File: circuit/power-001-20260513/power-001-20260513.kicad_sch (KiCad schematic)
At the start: 47 parts, among them J1 VIN, Q1 NMOS, Q2 PMOS, SW1 SW_SPST, SW2 SW_SPDT, SW3 SW_SPDT, SW4 SW_SPDT, U1 PIC12F683-xSN

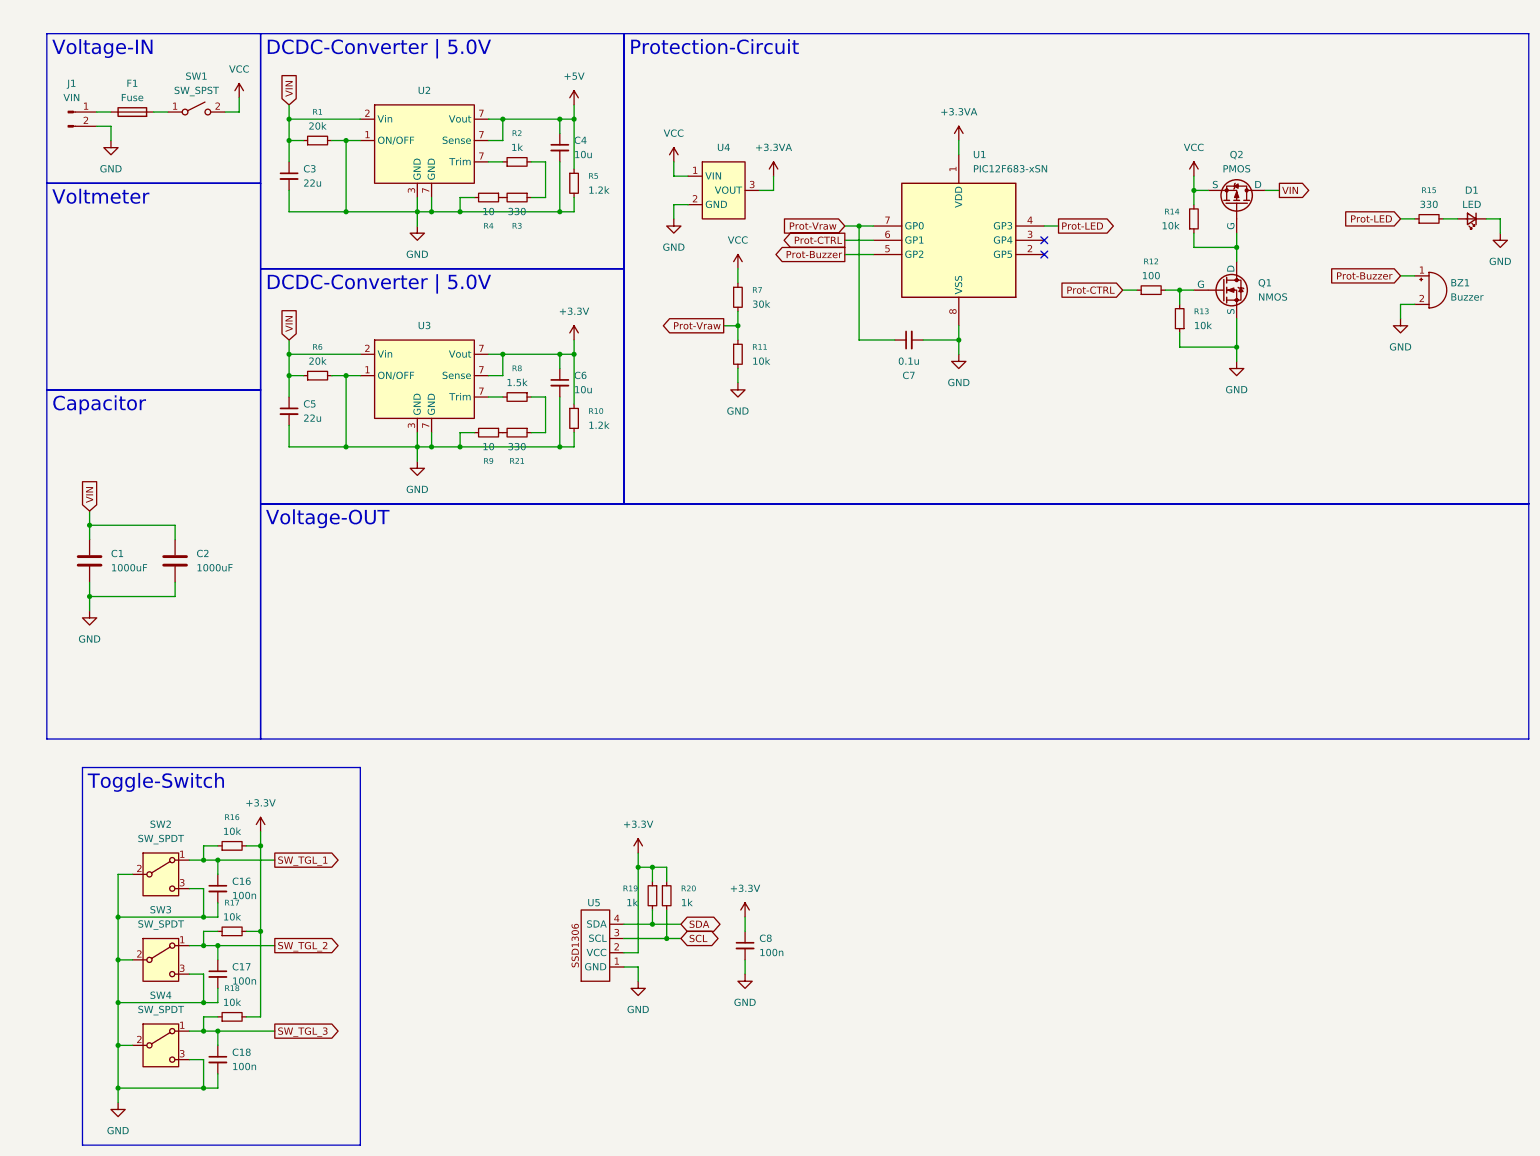
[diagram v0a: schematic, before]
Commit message: Update 電源基板の回路図完成・OKLのシンボルのピン番号が被っていたので修正
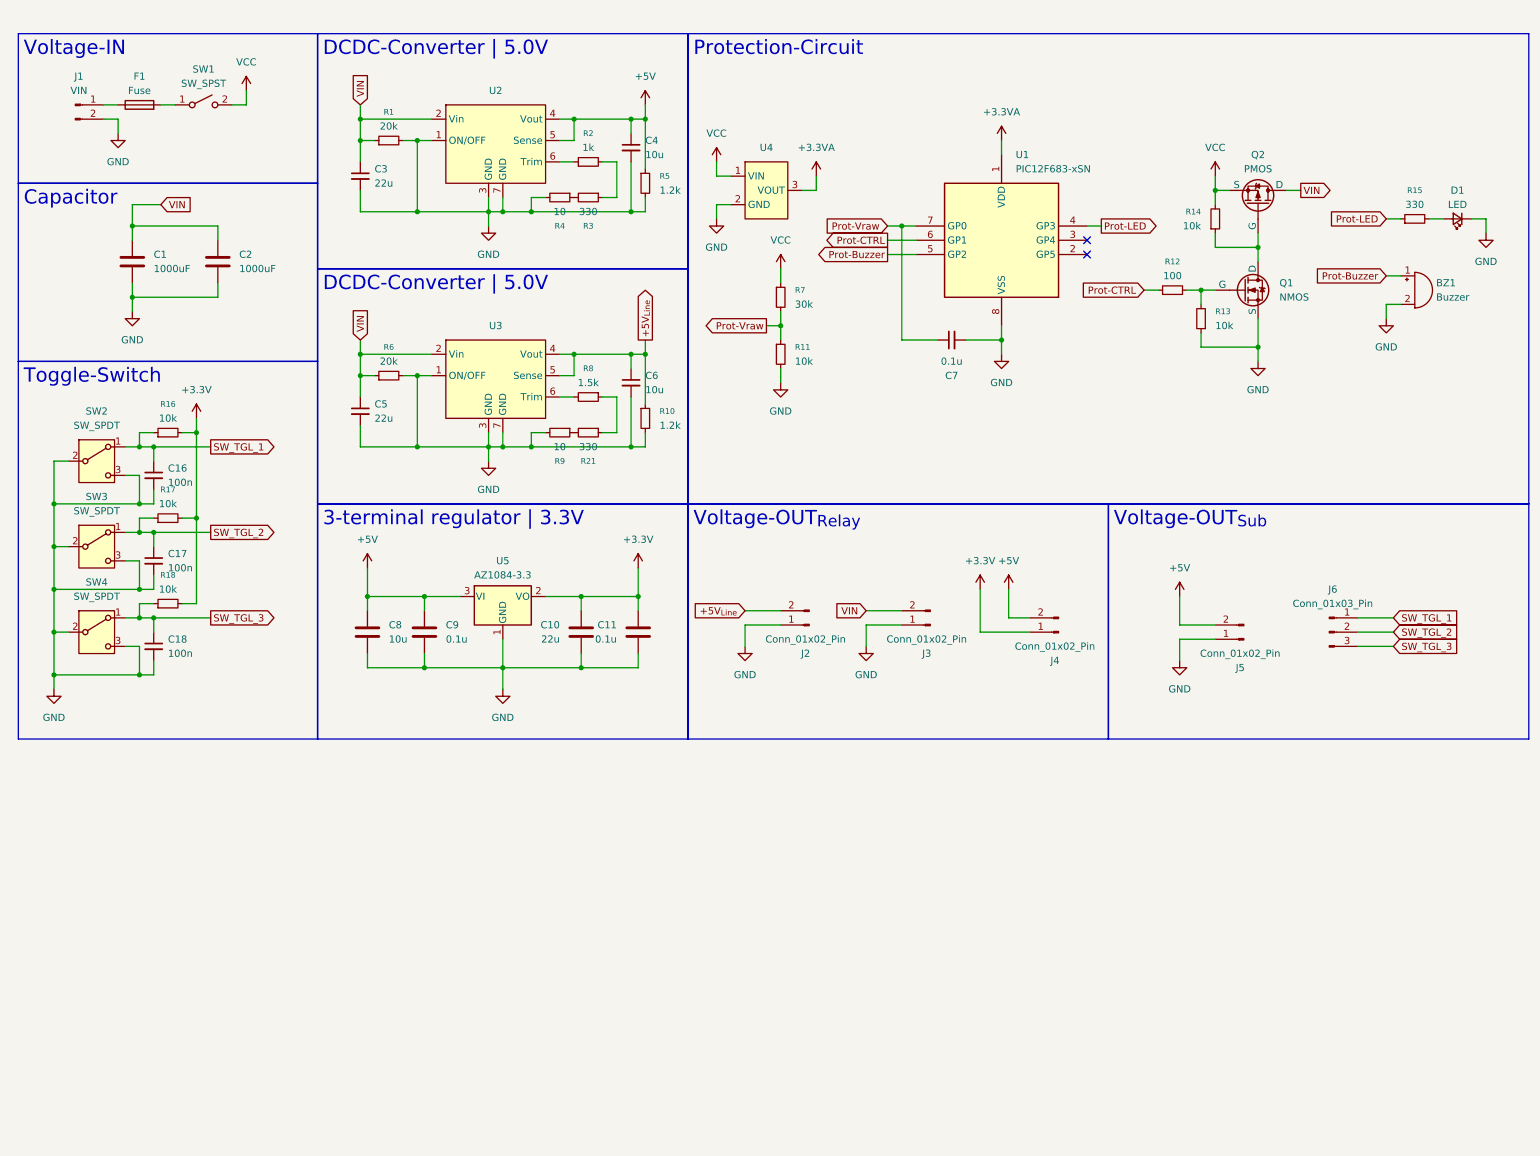
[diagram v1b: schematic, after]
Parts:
- removed C8: 100n, Capacitor_SMD:C_0805_2012Metric, symbol Device:C_Small
- removed R19, R20: 1k, Resistor_SMD:R_0805_2012Metric, symbol Device:R_Small
- removed U5: (no value), symbol @Thrive_symbol_sub:SSD1306
- added C10: 22u, symbol Device:C
- added C11, C9: 0.1u, symbol Device:C
- added C8: 10u, symbol Device:C
- added J2, J3, J4, J5: Conn_01x02_Pin, symbol Connector:Conn_01x02_Pin
- added J6: Conn_01x03_Pin, symbol Connector:Conn_01x03_Pin
- added U5: AZ1084-3.3, symbol Regulator_Linear:AZ1084-3.3
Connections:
- net +3.3V: now also C10.1, C11.1, J4.1 (Pin_1), U5.2 (VO); no longer C6.1, R10.1, U3.7 (Trim)
- net +5V: now also U2.4 (Vout), U2.5 (Sense), C8.1, C9.1, J4.2 (Pin_2), J5.2 (Pin_2), U5.3 (VI); no longer U2.7 (Trim)
- net GND: now also C10.2, C11.2, C8.2, C9.2, J2.1 (Pin_1), J3.1 (Pin_1), J5.1 (Pin_1), U5.1 (GND)
- net SW_TGL_1: now also J6.1 (Pin_1)
- net SW_TGL_2: now also J6.2 (Pin_2)
- net SW_TGL_3: now also J6.3 (Pin_3)
- net VIN: now also J3.2 (Pin_2)
- net at R2.1: now also U2.6 (Trim); no longer U2.7 (Trim)
- net at R8.2: now also U3.6 (Trim); no longer U3.7 (Trim)
- new net +5V_{Line}: C6.1, J2.2 (Pin_2), R10.1, U3.4 (Vout), U3.5 (Sense)
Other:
- moved on the sheet: BZ1, C1, C16, C17, C18, C2, C3, C4, C5, C6, C7, D1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

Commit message: Update 電源基板をちょっと進めた
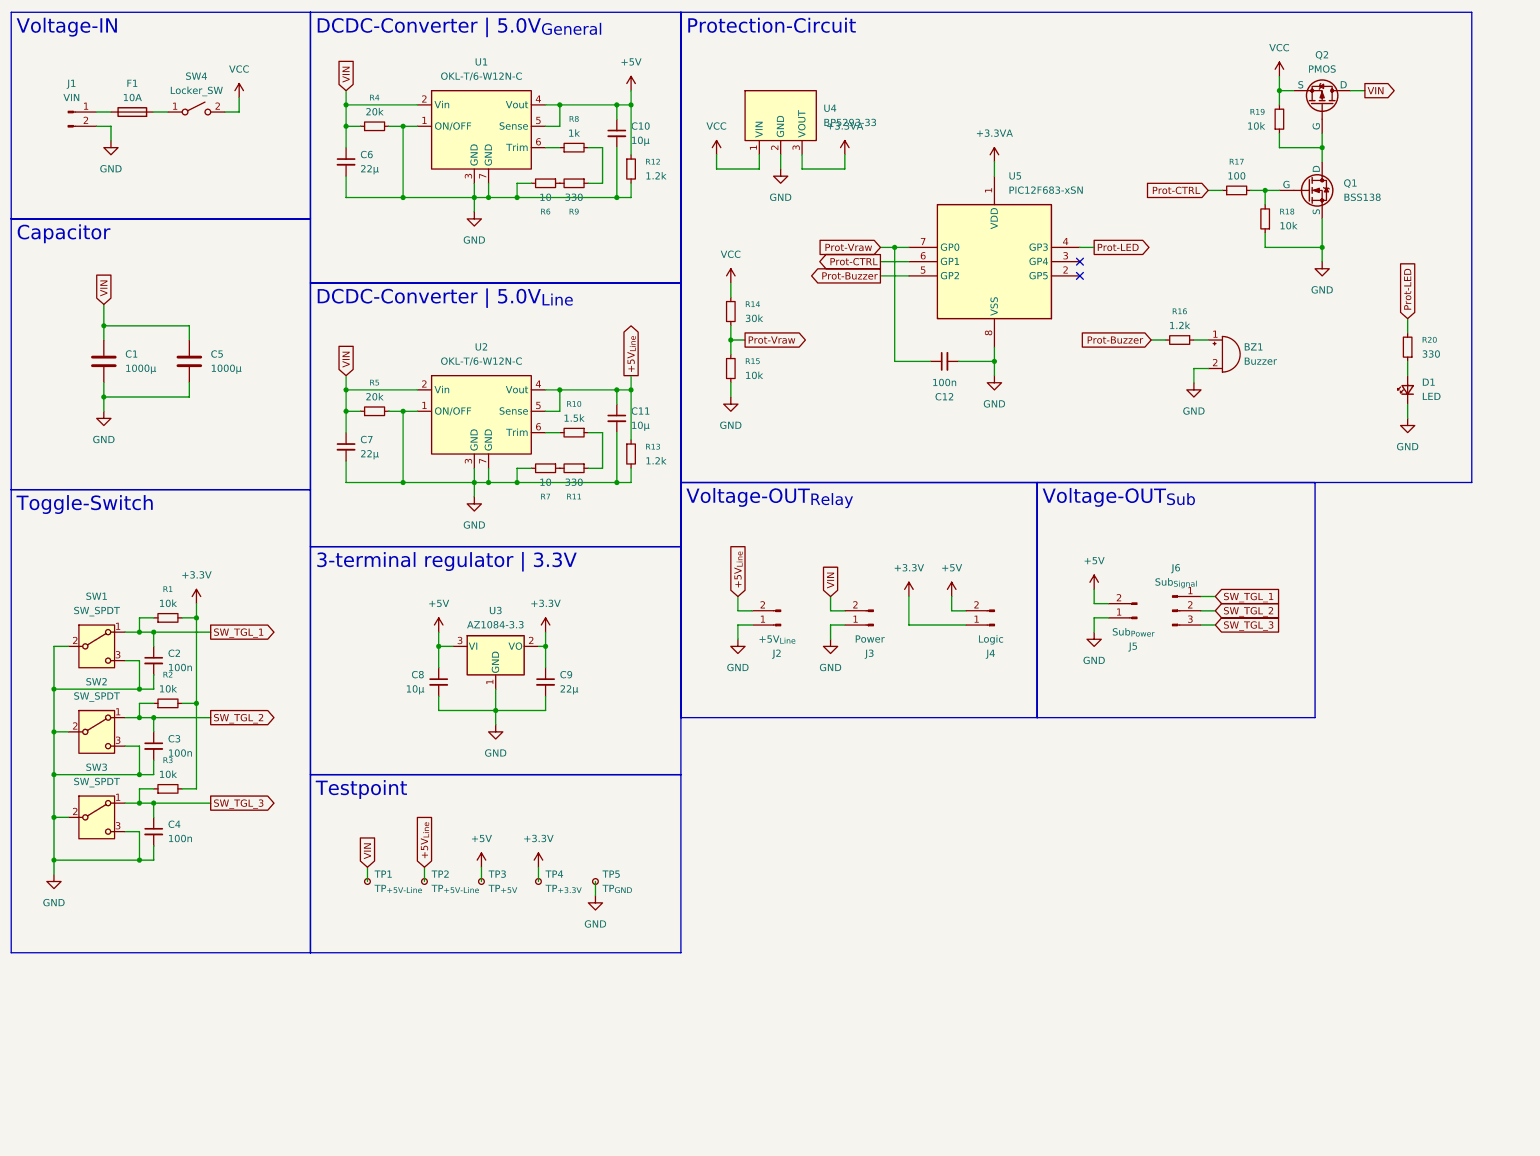
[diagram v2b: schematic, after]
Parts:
- removed C10: 22u, symbol Device:C
- removed C11, C9: 0.1u, symbol Device:C
- removed C8: 10u, symbol Device:C
- removed U3: (no value), symbol @Thrive_symbol_power:OKL-T/6-W12N-C
- added C8: 10μ, Capacitor_SMD:C_0805_2012Metric, symbol Device:C_Small
- added C9: 22μ, Capacitor_SMD:C_0805_2012Metric, symbol Device:C_Small
- added R16: 1.2k, Resistor_SMD:R_0805_2012Metric, symbol Device:R_Small
- added TP1, TP2: TP_{+5V-Line}, symbol Connector:TestPoint_Small
- added TP3: TP_{+5V}, symbol Connector:TestPoint_Small
- added TP4: TP_{+3.3V}, symbol Connector:TestPoint_Small
- added TP5: TP_{GND}, symbol Connector:TestPoint_Small
- added U1: OKL-T/6-W12N-C, @Thrive_footprint_power:OKL-T6-W12N-C, symbol @Thrive_symbol_power:OKL-T/6-W12N-C
- BZ1: footprint (none) -> @Thrive_footprint_power:PKM13EPYH4000-A0
- C1: value 1000uF -> 1000μ
- C10: renamed from C4; value 10u -> 10μ; footprint (none) -> Capacitor_SMD:C_0805_2012Metric
- C11: renamed from C6; value 10u -> 10μ; footprint (none) -> Capacitor_SMD:C_0805_2012Metric
- C12: renamed from C7; value 0.1u -> 100n; footprint (none) -> Capacitor_SMD:C_0805_2012Metric
- C5: renamed from C2; value 1000uF -> 1000μ
- C6: renamed from C3; value 22u -> 22μ; footprint (none) -> Capacitor_SMD:C_0805_2012Metric
- C7: renamed from C5; value 22u -> 22μ; footprint (none) -> Capacitor_SMD:C_0805_2012Metric
- D1: footprint (none) -> Capacitor_SMD:C_0603_1608Metric
- F1: value Fuse -> 10A
- J2: value Conn_01x02_Pin -> +5V_{Line}
- J3: value Conn_01x02_Pin -> Power
- J4: value Conn_01x02_Pin -> Logic
- J5: value Conn_01x02_Pin -> Sub_{Power}
- J6: value Conn_01x03_Pin -> Sub_{Signal}
- Q1: value NMOS -> BSS138; footprint (none) -> Package_TO_SOT_SMD:TSOT-23
- R10: renamed from R8; footprint (none) -> Resistor_SMD:R_0805_2012Metric
- R11: renamed from R21; footprint (none) -> Resistor_SMD:R_0805_2012Metric
- R12: renamed from R5; footprint (none) -> Resistor_SMD:R_0805_2012Metric
- R13: renamed from R10; footprint (none) -> Resistor_SMD:R_0805_2012Metric
- R14: renamed from R7; footprint (none) -> Resistor_SMD:R_0805_2012Metric
- R15: renamed from R11; footprint (none) -> Resistor_SMD:R_0805_2012Metric
- R17: renamed from R12; footprint (none) -> Resistor_SMD:R_0805_2012Metric
- R18: renamed from R13; footprint (none) -> Resistor_SMD:R_0805_2012Metric
- R19: renamed from R14; footprint (none) -> Resistor_SMD:R_0805_2012Metric
- R20: renamed from R15; footprint (none) -> Resistor_SMD:R_0805_2012Metric
- R4: renamed from R1; footprint (none) -> Resistor_SMD:R_0805_2012Metric
- R5: renamed from R6; footprint (none) -> Resistor_SMD:R_0805_2012Metric
- R6: renamed from R4; footprint (none) -> Resistor_SMD:R_0805_2012Metric
- R7: renamed from R9; footprint (none) -> Resistor_SMD:R_0805_2012Metric
- R8: renamed from R2; footprint (none) -> Resistor_SMD:R_0805_2012Metric
- R9: renamed from R3; footprint (none) -> Resistor_SMD:R_0805_2012Metric
- SW4: renamed from SW1; value SW_SPST -> Locker_SW
- U2: value (none) -> OKL-T/6-W12N-C; footprint (none) -> @Thrive_footprint_power:OKL-T6-W12N-C
- U3: renamed from U5; footprint (none) -> Package_TO_SOT_SMD:TO-252-2
- U4: value (none) -> BP5293-33
- renumbered C16 to C2, C17 to C3, C18 to C4, R16 to R1, R17 to R2, R18 to R3, SW2 to SW1, SW3 to SW2, SW4 to SW3, U1 to U5
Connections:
- net +3.3V: now also C9.1, TP4.1
- net +5V: now also C8.1, TP3.1, U1.4 (Vout), U1.5 (Sense); no longer U2.4 (Vout), U2.5 (Sense)
- net +5V_{Line}: now also U2.4 (Vout), U2.5 (Sense), TP2.1
- net GND: now also C8.2, C9.2, TP5.1, U1.1 (ON/OFF), U1.3 (GND), U1.7 (GND)
- net Prot-Buzzer: now also R16.2; no longer BZ1.1 (+)
- net Prot-LED: now also R20.2; no longer R20.1
- net VIN: now also TP1.1, U1.2 (Vin)
- net at R8.1: now also U1.6 (Trim); no longer U2.6 (Trim)
- net at D1.2 (A): now also R20.1; no longer R20.2
- net at R10.2: now also U2.6 (Trim)
- new net: BZ1.1 (+), R16.1
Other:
- moved on the sheet: BZ1, C1, C10, C11, C12, C2, C3, C4, C5, C6, C7, F1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

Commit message: Update ラインセンサ基板回路図更新
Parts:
- C1, C5: footprint (none) -> Capacitor_THT:CP_Radial_D10.0mm_P5.00mm
- J2, J3, J4, J5: footprint (none) -> Connector_AMASS:AMASS_XT30PW-F_1x02_P2.50mm_Horizontal
- J6: footprint (none) -> Connector_PinHeader_2.54mm:PinHeader_1x03_P2.54mm_Horizontal
- Q2: footprint (none) -> Package_TO_SOT_SMD:TO-252-2
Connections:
- net VIN: now also Q2.2 (D); no longer Q2.1 (D)
- net at Q1.1 (D), R19.1: now also Q2.1 (G); no longer Q2.2 (G)
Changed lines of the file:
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@@
 			)
 		)
-		(property "Footprint" ""
+		(property "Footprint" "Connector_AMASS:AMASS_XT30PW-F_1x02_P2.50mm_Horizontal"
 			(at 213.36 120.65 0)
 			(hide yes)
@@
 			)
 		)
-		(property "Footprint" ""
+		(property "Footprint" "Connector_AMASS:AMASS_XT30PW-F_1x02_P2.50mm_Horizontal"
 			(at 149.86 121.92 0)
 			(hide yes)
@@
 			)
 		)
-		(property "Footprint" ""
+		(property "Footprint" "Package_TO_SOT_SMD:TO-252-2"
 			(at 248.92 24.13 0)
 			(hide yes)
@@
 			)
 		)
-		(property "Footprint" ""
+		(property "Footprint" "Capacitor_THT:CP_Radial_D10.0mm_P5.00mm"
 			(at 30.1752 78.74 0)
 			(hide yes)
@@
 			)
 		)
-		(property "Footprint" ""
+		(property "Footprint" "Connector_PinHeader_2.54mm:PinHeader_1x03_P2.54mm_Horizontal"
 			(at 219.71 119.38 0)
 			(hide yes)
@@
 			)
 		)
-		(property "Footprint" ""
+		(property "Footprint" "Connector_AMASS:AMASS_XT30PW-F_1x02_P2.50mm_Horizontal"
 			(at 187.96 121.92 0)
 			(hide yes)
@@
 			)
 		)
-		(property "Footprint" ""
+		(property "Footprint" "Capacitor_THT:CP_Radial_D10.0mm_P5.00mm"
 			(at 45.4152 78.74 0)
 			(hide yes)
@@
 			)
 		)
-		(property "Footprint" ""
+		(property "Footprint" "Connector_AMASS:AMASS_XT30PW-F_1x02_P2.50mm_Horizontal"
 			(at 166.37 121.92 0)
 			(hide yes)

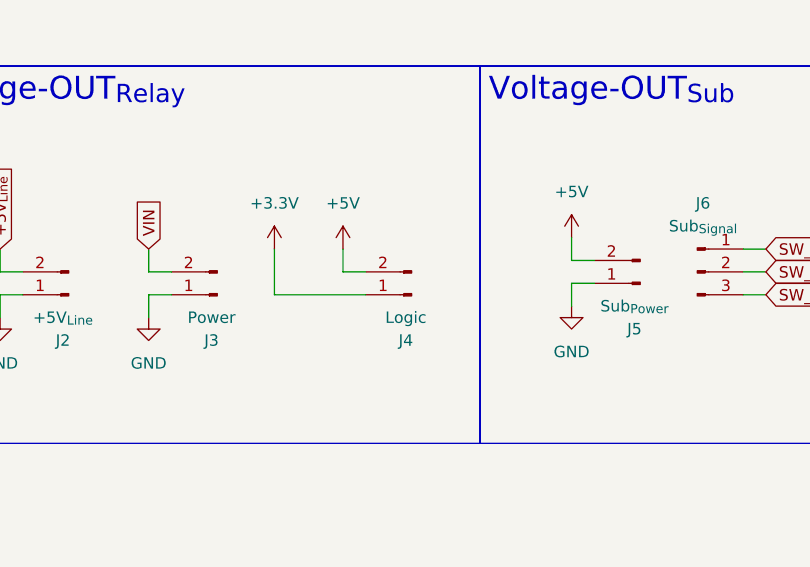
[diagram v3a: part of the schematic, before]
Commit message: Update 電源基板のボード図を編集し始めた
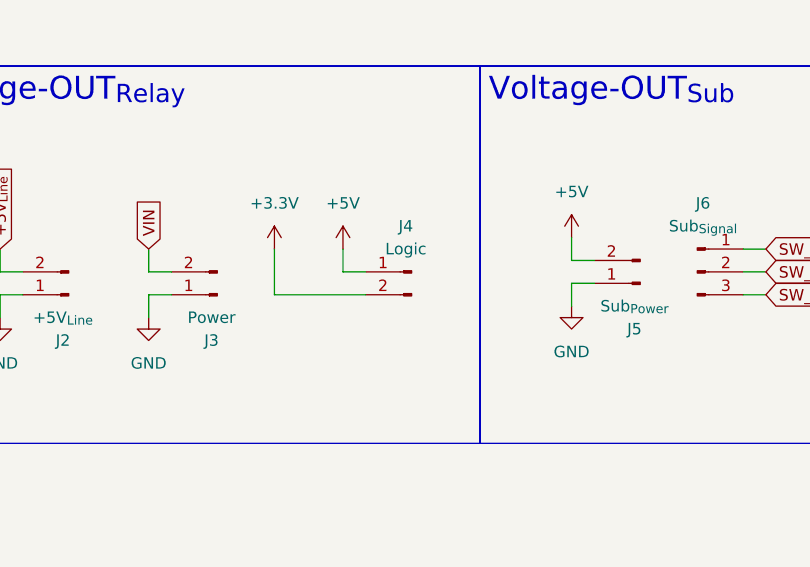
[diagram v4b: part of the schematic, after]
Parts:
- U4: footprint (none) -> @Thrive_footprint_power:BP5293-33
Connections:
- net +3.3V: now also J4.2 (Pin_2); no longer J4.1 (Pin_1)
- net +5V: now also J4.1 (Pin_1); no longer J4.2 (Pin_2)
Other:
- moved on the sheet: J4
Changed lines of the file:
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@@
 			)
 		)
-		(property "Footprint" ""
+		(property "Footprint" "@Thrive_footprint_power:BP5293-33"
 			(at 149.86 26.67 0)
 			(hide yes)
@@
 	(symbol
 		(lib_id "Connector:Conn_01x02_Pin")
-		(at 187.96 121.92 180)
+		(at 187.96 119.38 0)
+		(mirror y)
 		(unit 1)
 		(body_style 1)
@@
 		(dnp no)
 		(property "Reference" "J4"
-			(at 187.325 127 0)
+			(at 187.325 114.3 0)
 			(show_name no)
 			(do_not_autoplace no)
@@
 		)
 		(property "Value" "Logic"
-			(at 187.325 124.46 0)
+			(at 187.325 116.84 0)
 			(show_name no)
 			(do_not_autoplace no)
@@
 		)
 		(property "Footprint" "Connector_AMASS:AMASS_XT30PW-F_1x02_P2.50mm_Horizontal"
-			(at 187.96 121.92 0)
+			(at 187.96 119.38 0)
 			(hide yes)
 			(show_name no)
@@
 		)
 		(property "Datasheet" ""
-			(at 187.96 121.92 0)
+			(at 187.96 119.38 0)
 			(hide yes)
 			(show_name no)
@@
 		)
 		(property "Description" "Generic connector, single row, 01x02, script generated"
-			(at 187.96 121.92 0)
+			(at 187.96 119.38 0)
 			(hide yes)
 			(show_name no)
